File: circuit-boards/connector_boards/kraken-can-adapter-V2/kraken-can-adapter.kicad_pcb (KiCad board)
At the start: 2 copper layers, 44.3 x 25.3 mm, 4 parts, among them J1 CAN, J2 CAN, J3 CAN_L, J4 CAN_H

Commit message: Kraken Can V2
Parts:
- moved J2 34.5 mm to (126.9, 118.5), turned to -135 degrees
- moved J1 34.0 mm to (87.4, 120.3), turned to 135 degrees
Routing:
- net /CAN_L: track 45.3 -> 47.2 mm
- net /CAN_H: track 45.5 -> 47.2 mm
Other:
- board size 44.3 x 25.3 mm -> 55.8 x 21.6 mm
- board text added: "KRAKEN CAN ADAPTER V2 2024"
- board text removed: "KRAKEN CAN ADAPTER V1 2024"

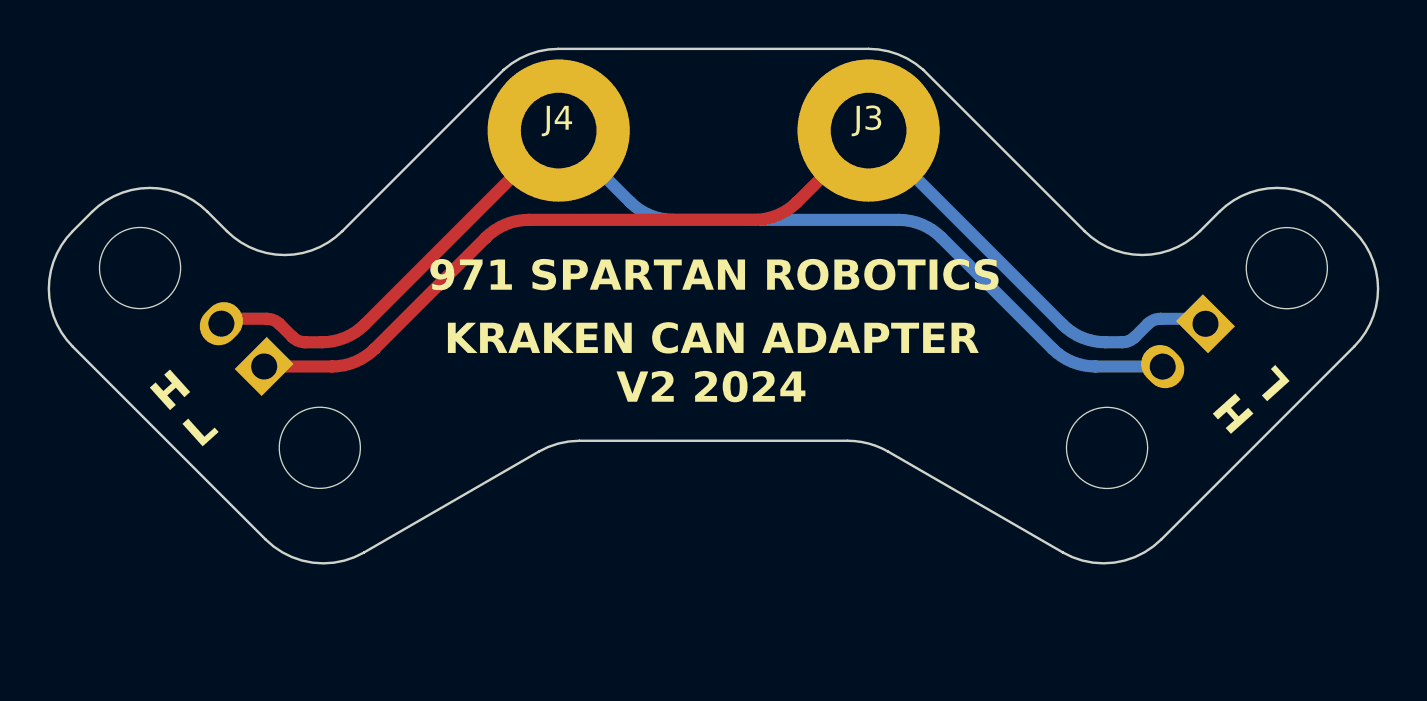
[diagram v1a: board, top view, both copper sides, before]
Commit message: Fixed kraken-can-adapter V2.
Signed-off-by: Scott Berman <scott.berman@bluerivertech.com>
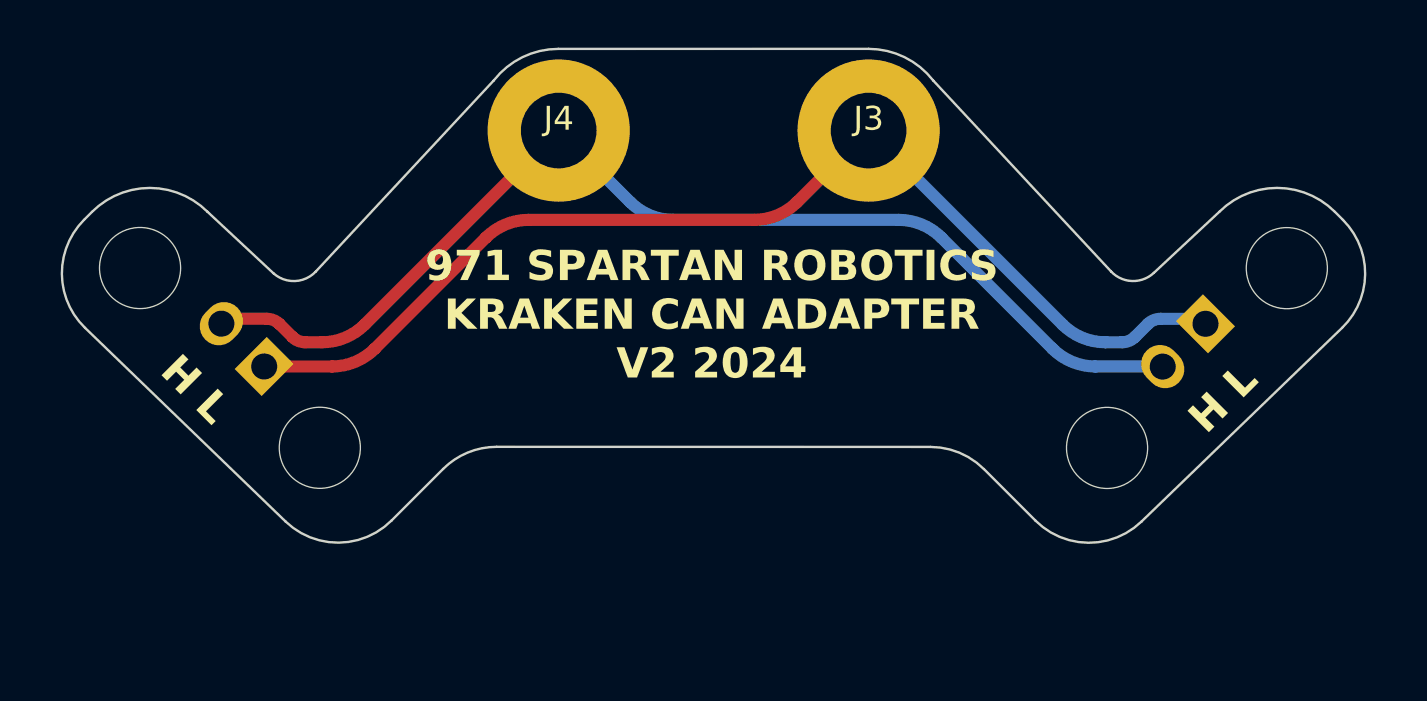
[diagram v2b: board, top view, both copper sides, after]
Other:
- board size 55.8 x 21.6 mm -> 54.7 x 20.7 mm
- board text added: "0.3937 mils"
- board text added: "1.37795 mils"
- board text added: "2153.08 mils x 815.97 mils"
- board text added: "59.44882 mils"
- board text added: "971 SPARTAN ROBOTICS KRAKEN CAN ADAPTER V2 2024"
- board text added: "BACK"
- board text added: "Black"
- board text added: "Dielectric 1"
- board text added: "FRONT"
- board text removed: "0.3937007874 mils"
- board text removed: "1.377952756 mils"
- board text removed: "1743.72 mils x 853.80 mils"
- board text removed: "59.4488189 mils"
- board text removed: "971 SPARTAN ROBOTICS"
- board text removed: "Dielectric"
- board text removed: "Green"
- board text removed: "KRAKEN CAN ADAPTER V2 2024"
